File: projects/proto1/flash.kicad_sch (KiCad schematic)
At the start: 4 parts, among them U3 SST39SF040, U4 SST39SF040

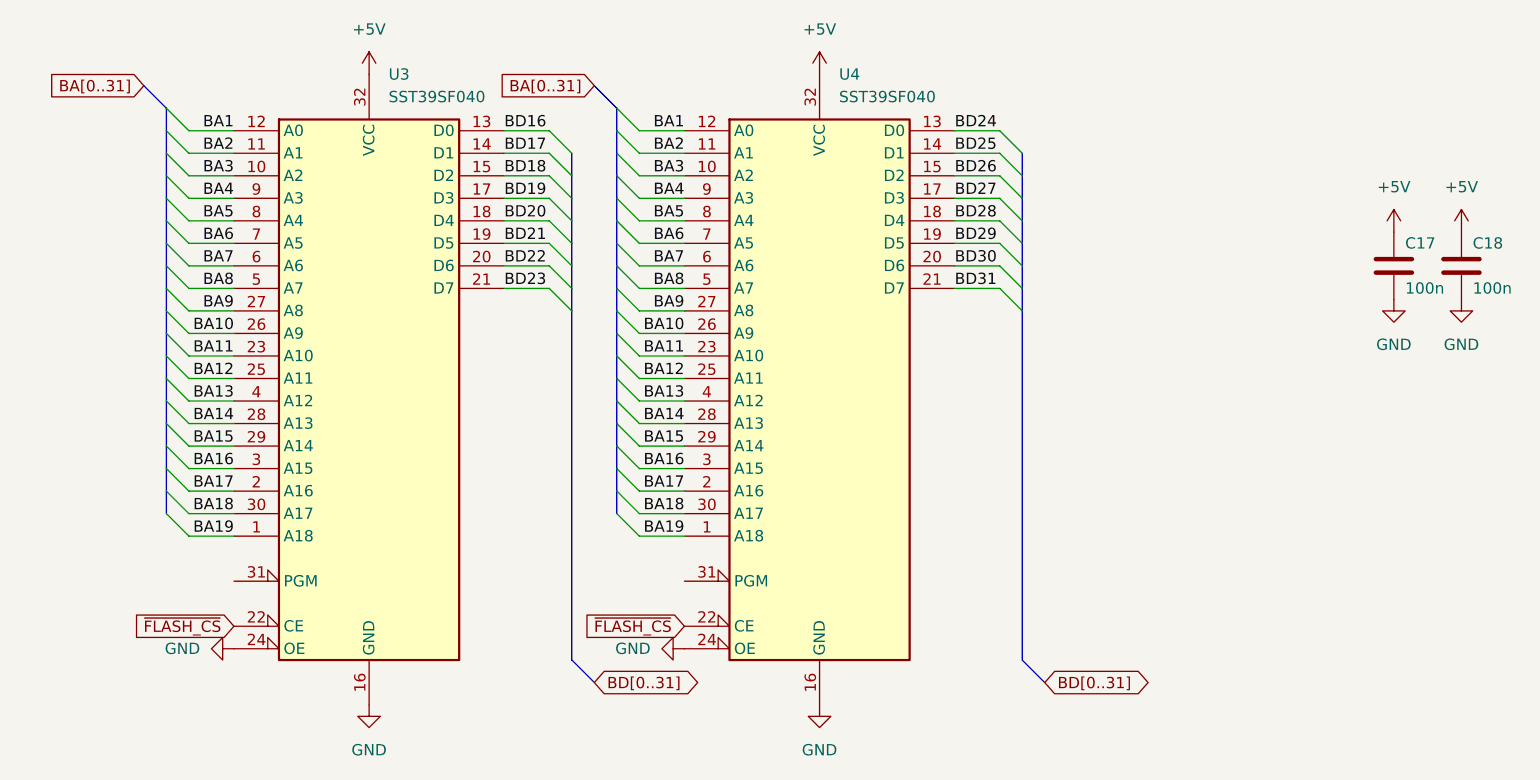
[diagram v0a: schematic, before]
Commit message: Renamed CMC to SCU, changed verification method to cocotb, and modified pcb schematic
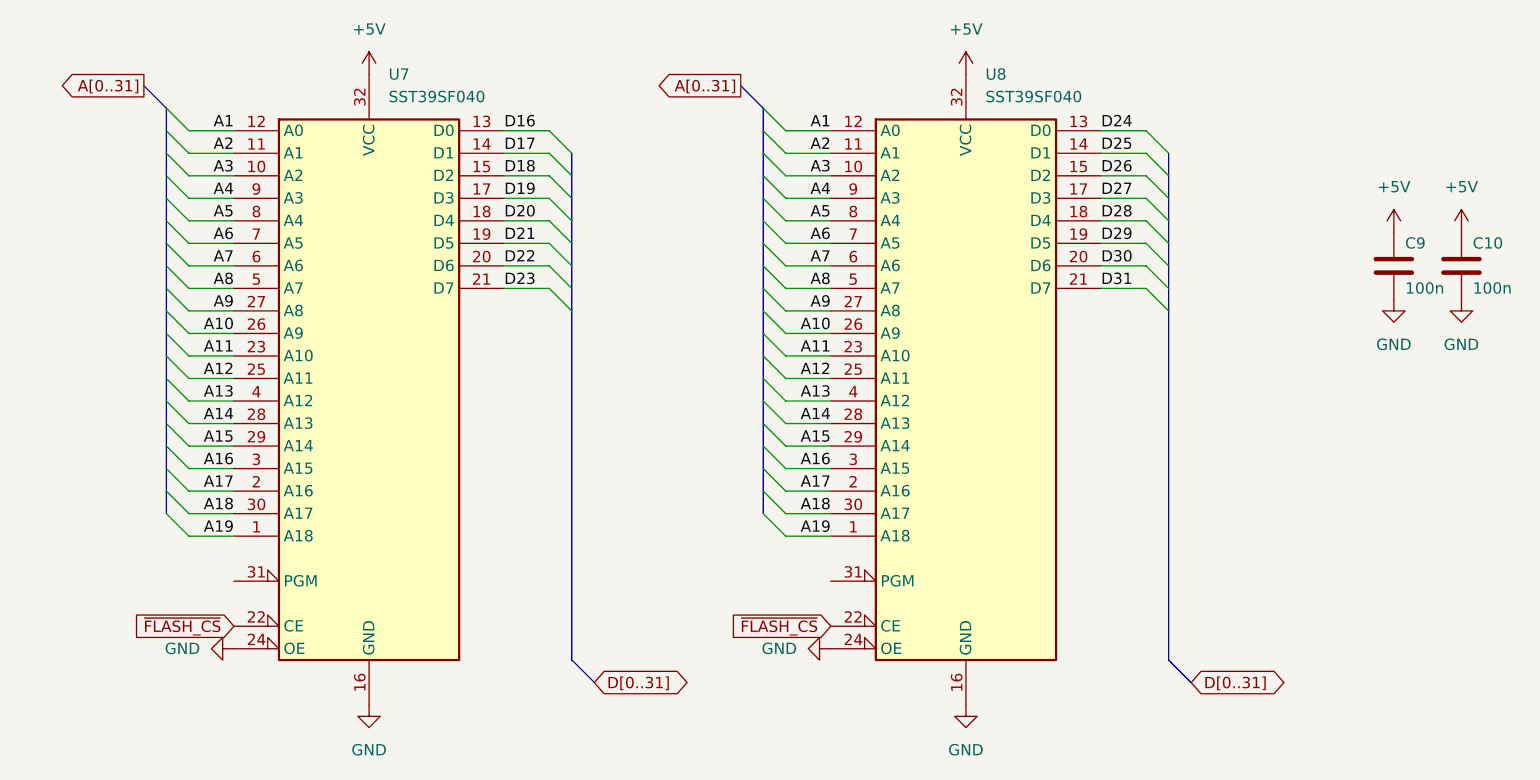
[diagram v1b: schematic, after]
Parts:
- renumbered C18 to C10, C17 to C9, U3 to U7, U4 to U8
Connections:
- net BA1 renamed A1
- net BA10 renamed A10
- net BA11 renamed A11
- net BA12 renamed A12
- net BA13 renamed A13
- net BA14 renamed A14
- net BA15 renamed A15
- net BA16 renamed A16
- net BA17 renamed A17
- net BA18 renamed A18
- net BA19 renamed A19
- net BA2 renamed A2
- net BA3 renamed A3
- net BA4 renamed A4
- net BA5 renamed A5
- net BA6 renamed A6
- net BA7 renamed A7
- net BA8 renamed A8
- net BA9 renamed A9
- net BD16 renamed D16
- net BD17 renamed D17
- net BD18 renamed D18
- net BD19 renamed D19
- net BD20 renamed D20
- net BD21 renamed D21
- net BD22 renamed D22
- net BD23 renamed D23
- net BD24 renamed D24
- net BD25 renamed D25
- net BD26 renamed D26
- net BD27 renamed D27
- net BD28 renamed D28
- net BD29 renamed D29
- net BD30 renamed D30
- net BD31 renamed D31
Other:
- moved on the sheet: U8
